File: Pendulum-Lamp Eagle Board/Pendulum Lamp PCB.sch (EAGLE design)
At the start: 36 parts, among them IC1 LM324N, IC2 7805TV, IC3 LM324N, U1 QRD1114, U2 QRD1114, U3 QRD1114, U4 QRD1114, U5 QRD1114, U6 QRD1114, U7 QRD1114, U8 QRD1114

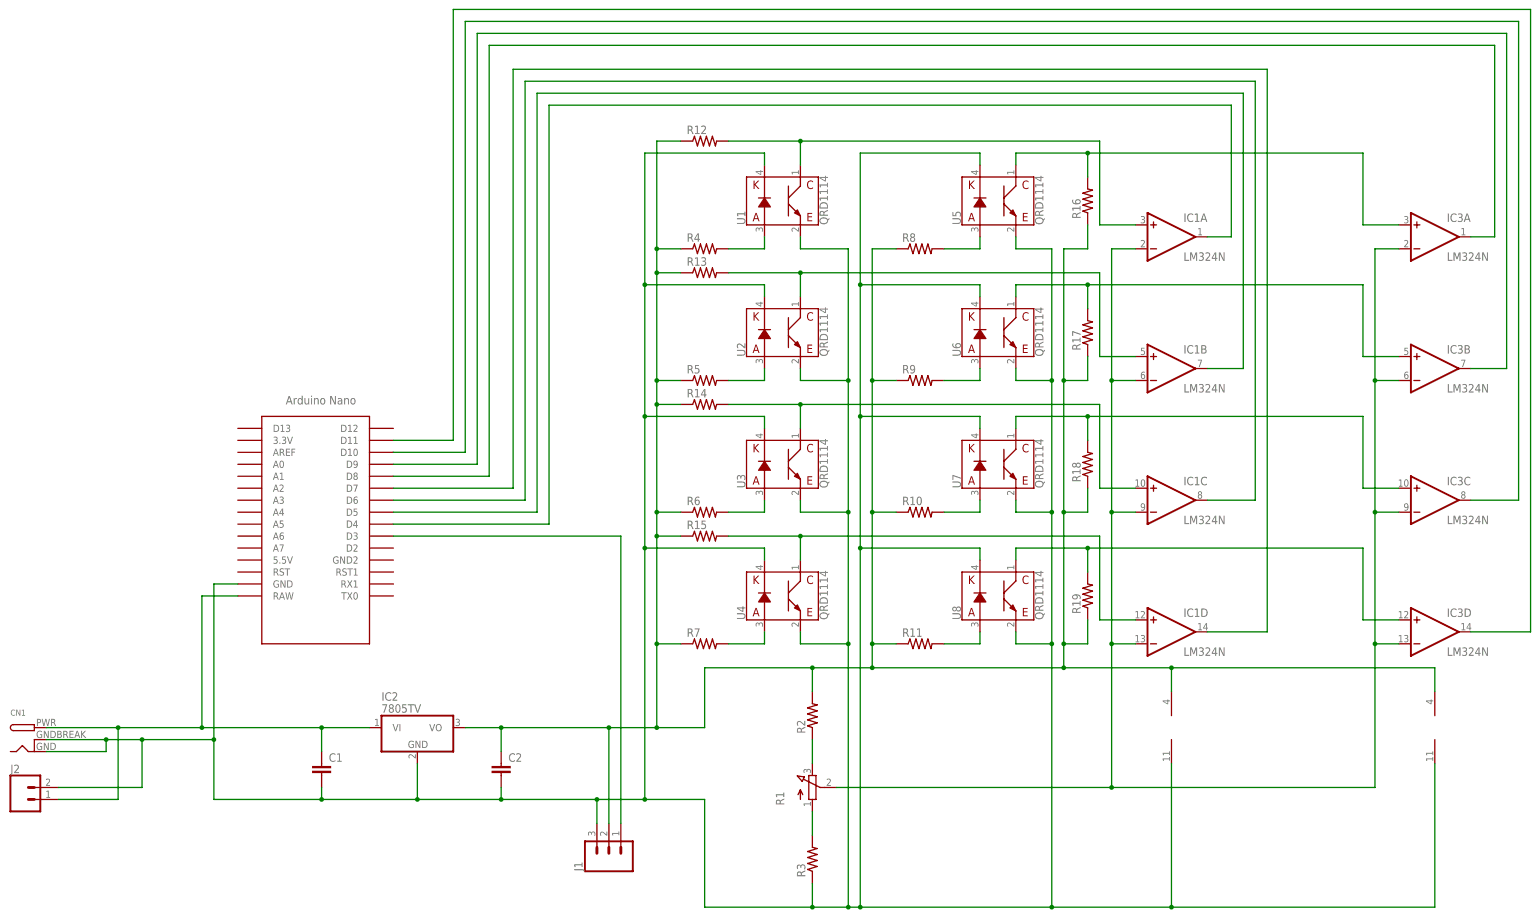
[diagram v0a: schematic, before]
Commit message: Some mechanical references modified
Re opened assembly files, re adjusts paths to referenced assemby. Made a layout to determine the pcb form factor based on the mechanism. Gosh, maybe I shoud migrate to Fusion 360
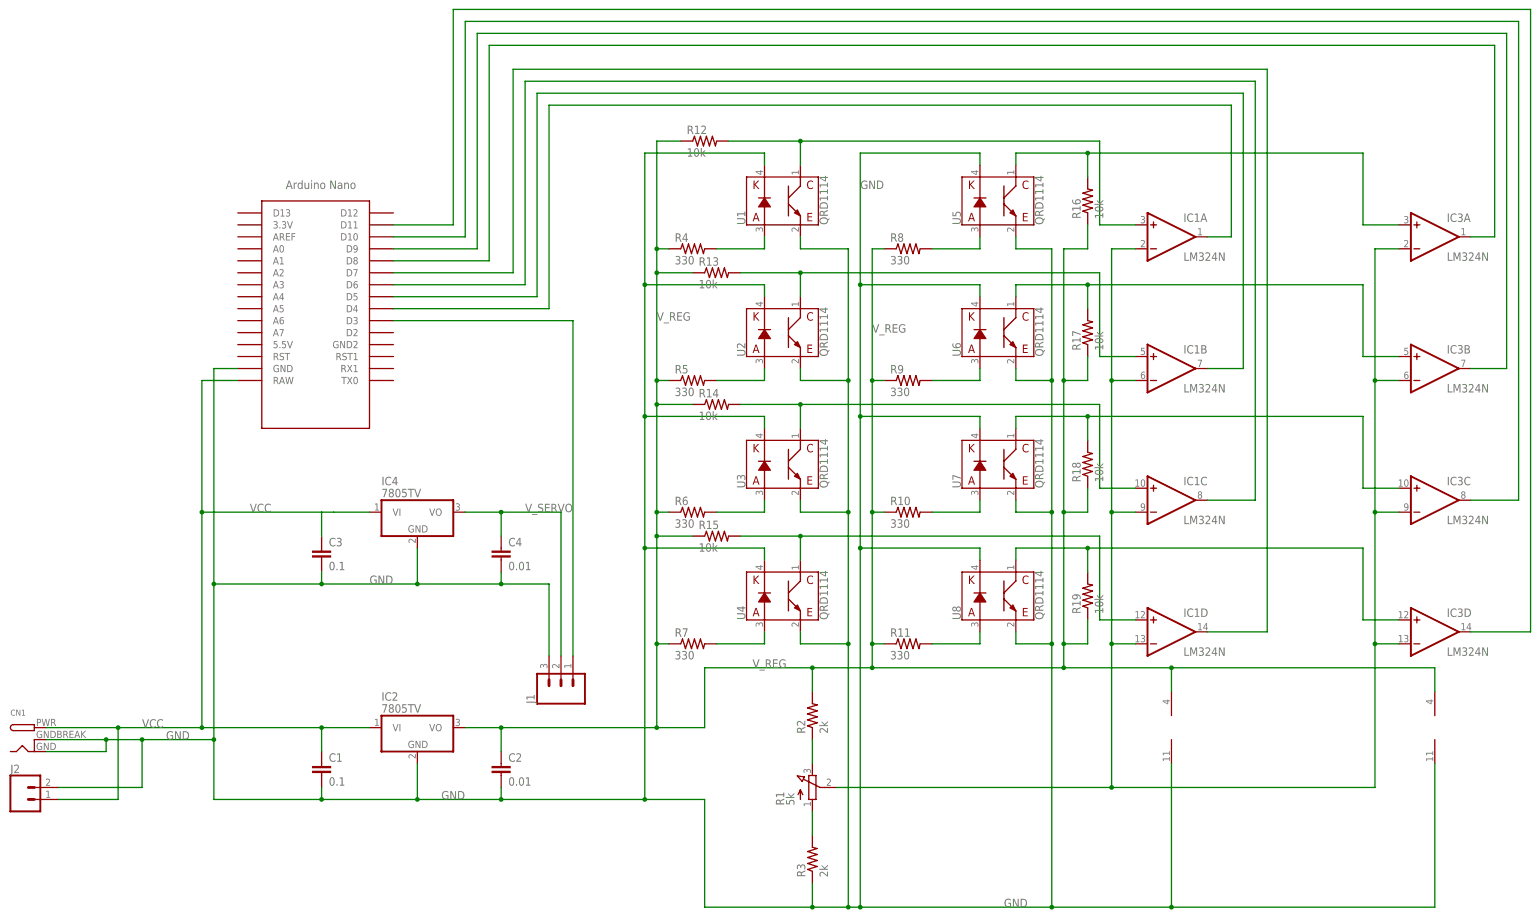
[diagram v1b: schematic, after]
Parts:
- added C3: 0.1, rcl:C-EU025-030X050
- added C4: 0.01, rcl:C-EU025-030X050
- added IC4: 7805TV, linear:7805TV
- C1: value (none) -> 0.1
- C2: value (none) -> 0.01
- R1: value (none) -> 5k
- R10, R11, R4, R5, R6, R7, R8, R9: value (none) -> 330
- R12, R13, R14, R15, R16, R17, R18, R19: value (none) -> 10k
- R2, R3: value (none) -> 2k
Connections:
- removed net N$1: C1.1, CN1.PWR, IC2.VI, J2.1, U$1.RAW
- removed net N$2: C1.2, C2.2, CN1.GND, CN1.GNDBREAK, IC1P.V-, IC2.GND, IC3P.V-, J1.3, J2.2, R3.1, U$1.GND, U1.E, U1.K, U2.E, U2.K, U3.E, U3.K, U4.E, U4.K, U5.E, U5.K, U6.E, U6.K, U7.E, U7.K, U8.E, U8.K
- removed net N$4: C2.1, IC1P.V+, IC2.VO, IC3P.V+, J1.2, R10.1, R11.1, R12.1, R13.1, R14.1, R15.1, R16.1, R17.1, R18.1, R19.1, R2.2, R4.1, R5.1, R6.1, R7.1, R8.1, R9.1
- new net GND: C1.2, C2.2, C3.2, C4.2, CN1.GND, CN1.GNDBREAK, IC1P.V-, IC2.GND, IC3P.V-, IC4.GND, J1.3, J2.2, R3.1, U$1.GND, U1.E, U1.K, U2.E, U2.K, U3.E, U3.K, U4.E, U4.K, U5.E, U5.K, U6.E, U6.K, U7.E, U7.K, U8.E, U8.K
- new net VCC: C1.1, C3.1, CN1.PWR, IC2.VI, IC4.VI, J2.1, U$1.RAW
- new net V_REG: C2.1, IC1P.V+, IC2.VO, IC3P.V+, R10.1, R11.1, R12.1, R13.1, R14.1, R15.1, R16.1, R17.1, R18.1, R19.1, R2.2, R4.1, R5.1, R6.1, R7.1, R8.1, R9.1
- new net V_SERVO: C4.1, IC4.VO, J1.2
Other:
- moved on the sheet: J1, R10, R11, R13, R14, R15, R4, R5, R6, R7, R8, R9

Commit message: PCB board finished
Main pcb board finished. Some solid works parts modied
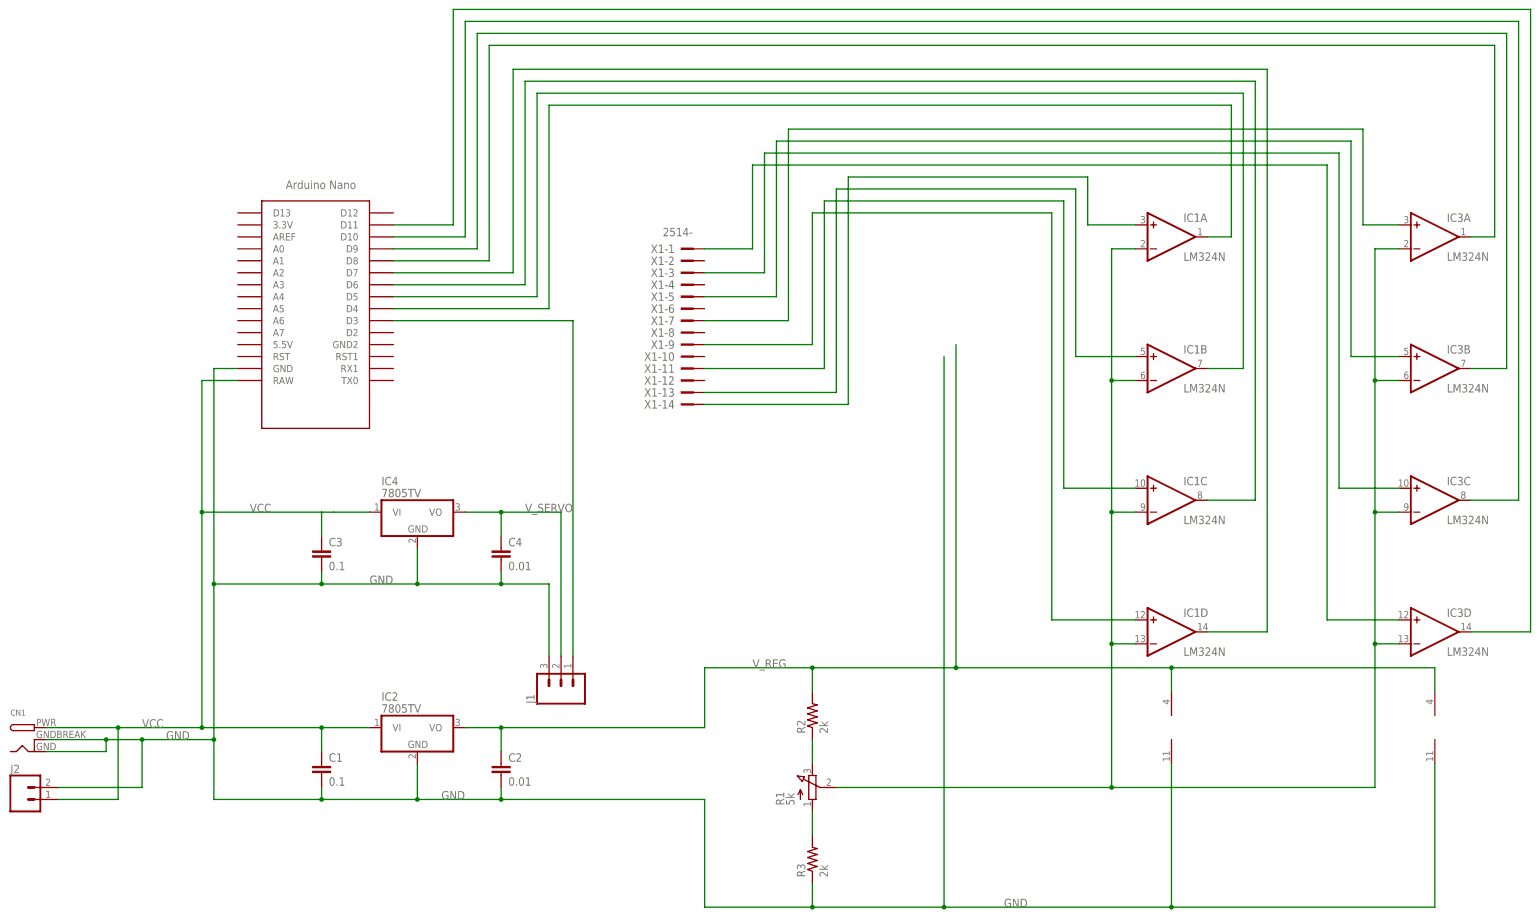
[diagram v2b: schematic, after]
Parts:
- removed R10, R11, R4, R5, R6, R7, R8, R9: 330, rcl:R-US_0204/7
- removed R12, R13, R14, R15, R16, R17, R18, R19: 10k, rcl:R-US_0204/7
- removed U1, U2, U3, U4, U5, U6, U7, U8: QRD1114, SparkFun-Sensors:QRD1114
- added X1: 2514-, con-3m:2514-
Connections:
- removed net N$20: R8.2, U5.A
- removed net N$22: R10.2, U7.A
- removed net N$23: R11.2, U8.A
- removed net N$27: IC3C.+IN, R18.2, U7.C
- removed net N$28: IC3B.+IN, R17.2, U6.C
- removed net N$29: IC3A.+IN, R16.2, U5.C
- removed net N$30: IC1D.+IN, R15.2, U4.C
- removed net N$31: IC1C.+IN, R14.2, U3.C
- removed net N$32: IC3D.+IN, R19.2, U8.C
- removed net N$33: IC1B.+IN, R13.2, U2.C
- removed net N$34: IC1A.+IN, R12.2, U1.C
- new net N$1: IC1A.+IN, X1-14.KL
- new net N$2: IC3B.+IN, X1-5.KL
- new net N$4: IC3C.+IN, X1-3.KL
- net GND: no longer U1.E, U1.K, U2.E, U2.K, U3.E, U3.K, U4.E, U4.K, U5.E, U5.K, U6.E, U6.K, U7.E, U7.K, U8.E, U8.K
- net N$16: now also IC3D.+IN, X1-1.KL; no longer R4.2, U1.A
- net N$17: now also IC1D.+IN, X1-9.KL; no longer R5.2, U2.A
- net N$18: now also IC1B.+IN, X1-13.KL; no longer R6.2, U3.A
- net N$19: now also IC1C.+IN, X1-11.KL; no longer R7.2, U4.A
- net N$21: now also IC3A.+IN, X1-7.KL; no longer R9.2, U6.A
- net V_REG: no longer R10.1, R11.1, R12.1, R13.1, R14.1, R15.1, R16.1, R17.1, R18.1, R19.1, R4.1, R5.1, R6.1, R7.1, R8.1, R9.1
